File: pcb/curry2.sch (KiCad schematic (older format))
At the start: 6 parts

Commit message: Schematic almost done
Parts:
- added C? (x4): 10µF, symbol C
- added C? (x5): 0.1µF, symbol C
- added C? (x8): 4.7µF, symbol C
- added C?: 0.47µF, symbol C
- added C? (x2): 22pF, symbol C
- added IC?: ATMEGA88-A, TQFP32, symbol ATMEGA88-A
- added L? (x2): INDUCTOR, symbol INDUCTOR
- added X?: CRYSTAL, symbol CRYSTAL
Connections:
- net at U?.1 (3v3): now also L?.2
- net DB4: now reaches U?.10 (GPIO15)
- net DB5: now reaches U?.11 (GPIO17)
- net DB6: now reaches U?.12 (GPIO18)
- net DB7: now reaches U?.13 (GPIO27)
- net DB8: now reaches U?.15 (GPIO22)
- net DB9: now reaches U?.16 (GPIO23)
- net DB10: now reaches U?.18 (GPIO24)
- net DB11: now reaches U?.19 (GPIO10)
- net at U?.2 (5V): now also U?.4 (5V), L?.1
- net DB12: now reaches U?.21 (GPIO9)
- net DB13: now reaches U?.22 (GPIO25)
- net DB14: now reaches U?.23 (GPIO11)
- net DB15: now reaches U?.24 (GPIO8)
- net RD: now reaches U?.26 (GPIO7)
- net RD: now also U?.12 (RD)
- net SDA: now reaches U?.29 (GPIO28/I2C0_SDA)
- net SDA: now also IC?.27 ((PCINT12/SDA/ADC4)PC4)
- net BUSY/INT: now reaches U?.3 (GIPO2)
- net BUSY/INT: now also U?.35 (BUSY/INT), IC?.2 ((PCINT20/XCK/T0)PD4)
- net SCL: now reaches U?.30 (GPIO29/I2C0SCL)
- net SCL: now also IC?.28 ((PCINT14/SCL/ADC5)PC5)
- net CS: now reaches U?.31 (GPIO30)
- net CS: now also U?.13 (CS/FS)
- net DB0: now reaches U?.5 (GPIO3)
- net DB0: now also U?.33 (DB0)
- net GND: now reaches U?.6 (GND)
- net GND: now also U?.24 (DGND), C?.1, C?.1, C?.2, C?.2, C?.2, C?.2
- net DB1: now reaches U?.7 (GPIO4)
- net DB2: now reaches U?.8 (GPIO14)
- net DB3: now reaches U?.9 (GND)
- net HVSS: now reaches U?.1 (HVSS)
- net HVSS: now also C?.2, C?.2
- net RES: now reaches U?.10 (RESET)
- net RES: now also IC?.24 ((PCINT9/ADC1)PC1)
- net WR: now reaches U?.11 (REFN/WR)
- net WR: now also IC?.23 ((PCINT8/ADC0)PC0)
- net AVDD: now reaches U?.14 (AVDD)
- net AVDD: now also U?.4 (AVDD), U?.45 (AVDD), U?.52 (AVDD), U?.57 (AVDD), U?.61 (AVDD), C?.1, C?.1, C?.1, C?.1, C?.1, C?.1, C?.1, L?.2
- net AGND: now reaches U?.15 (AGND)
- net AGND: now also U?.44 (AGND), U?.5 (AGND), U?.51 (AGND), U?.55 (REFN), U?.58 (AGND), U?.62 (AGND), C?.1, C?.1, C?.2, C?.2, C?.2, C?.2
- net chAop/OUT2: now reaches U?.2 (CH_D1)
- net DVDD: now reaches U?.25 (DVDD)
- net DVDD: now also C?.1, C?.1, L?.1
- net RANGE: now reaches U?.34 (RANGE/XCLK)
- net RANGE: now also IC?.1 ((PCINT19/OC2B/INT1)PD3)
- net SLEEP: now reaches U?.36 (ASLEEP)
- net SLEEP: now also IC?.9 ((PCINT21/OC0B/T1)PD5)
- net CONVA: now reaches U?.37 (CONVST_A)
- net CONVA: now also IC?.12 ((PCINT0/CLKO/ICP1)PB0)
- net CONVB: now reaches U?.38 (CONVST_B)
- net CONVB: now also IC?.13 ((PCINT1/OC1A)PB1)
- net CONVC: now reaches U?.39 (CONVST_C)
- net CONVC: now also IC?.14 ((PCINT2/OC1B/~SS~)PB2)
- net CONVD: now reaches U?.40 (CONVST_D)
- net CONVD: now also IC?.15 ((PCINT3/OC2/MOSI)PB3)
- net HW: now reaches U?.41 (HW/SW)
- net HW: now also IC?.16 ((PCINT4/MISO)PB4)
- net chAop/OUT1: now reaches U?.42 (CH_A0)
- net chAop/OUT2: now reaches U?.47 (CH_A1)
- net HVDD: now reaches U?.48 (HVDD)
- net HVDD: now also C?.1, C?.1
- net chAop/OUT1: now reaches U?.49 (CH_B0)
- net chAop/OUT2: now reaches U?.54 (CH_B1)
- net at U?.56 (REFIO): now also C?.2
- net chAop/OUT2: now reaches U?.59 (CH_C1)
- net chAop/OUT1: now reaches U?.64 (CH_C0)
- net chAop/OUT1: now reaches U?.7 (CH_D0)
- net PAR: now reaches U?.8 (PAR_/SER)
- net PAR: now also IC?.26 ((PCINT11/ADC3)PC3)
- net STD: now reaches U?.9 (STDBY)
- net STD: now also IC?.25 ((PCINT10/ADC2)PC2)
- new net: C?.1, C?.2 (x3)
- new net: C?.2, IC?.7 ((PCINT6/XTAL1/TOSC1)PB6), X?.1
- new net: C?.2, IC?.8 ((PCINT7/XTAL2/TOSC2)PB7), X?.2
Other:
- moved on the sheet: C?, U?

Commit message: almost done rtc placed
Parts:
- added BT?: BATTERY, symbol BATTERY
- added C?: 1µF, symbol C
- added CON?: AVR-ISP-6, AVR-ISP-6, symbol AVR-ISP-6
- added L? (x3): INDUCTOR, symbol INDUCTOR
- added P?: CONN_2, symbol CONN_2
- added P?: CONN_4X2, symbol CONN_4X2
- added R? (x3): R, symbol R
- added U?: BQ32000, symbol BQ32000
- added X?: CRYSTAL, symbol CRYSTAL
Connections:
- net chAop/OUT1 is gone; now on net chAop/OUT1: U?.7 (CH_D0)
- net chAop/OUT2 is gone; now on net chAop/OUT2: U?.59 (CH_C1)
- net AVDD: now also L?.1, L?.1; no longer L?.2
- net CONVA: now also P?.7
- net CONVB: now also P?.5
- net CONVC: now also P?.3
- net CONVD: now also CON?.4, P?.1
- net DVDD: now also IC?.4 (VCC), IC?.6 (VCC), C?.1, R?.1, R?.1, R?.1, U?.8 (VCC)
- net GND: now also IC?.3 (GND), U?.20 (GND), U?.25 (GND), U?.33 (GND), U?.34 (GND), U?.35 (GND), BT?.2 (-), C?.2, U?.4 (GND)
- net HW: now also CON?.1
- net SCL: now also U?.6 (SCL)
- net SDA: now also U?.5 (SDA)
- net chAop/OUT1: no longer U?.42 (CH_A0)
- net chAop/OUT2: no longer U?.2 (CH_D1)
- net power/+5: now also P?.1 (P1)
- net power/Enable: now also IC?.30 ((PCINT16/RXD)PD0)
- net power/GND: now also P?.2 (PM)
- net at L?.2, U?.1 (3v3): now also U?.17 (3V3)
- net at L?.1, U?.2 (5V), U?.4 (5V): now also L?.1
- net at IC?.11 ((PCINT23/AIN1)PD7): now also P?.2, P?.8
- net at IC?.17 ((PCINT5/SCK)PB5): now also CON?.3
- net RST: now reaches IC?.29 ((PCINT14/~RESET~)PC6)
- net RST: now also CON?.5, R?.2
- new net: L?.2, L?.2
- new net: U?.2 (OSCI), X?.2
- new net: BT?.1 (+), U?.3 (VBAT)
- new net: U?.3 (VBAT), X?.1
- new net chAop/OUT1: U?.42 (CH_A0)
- new net chAop/OUT2: U?.2 (CH_D1)
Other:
- moved on the sheet: C?, IC?, L?, X?

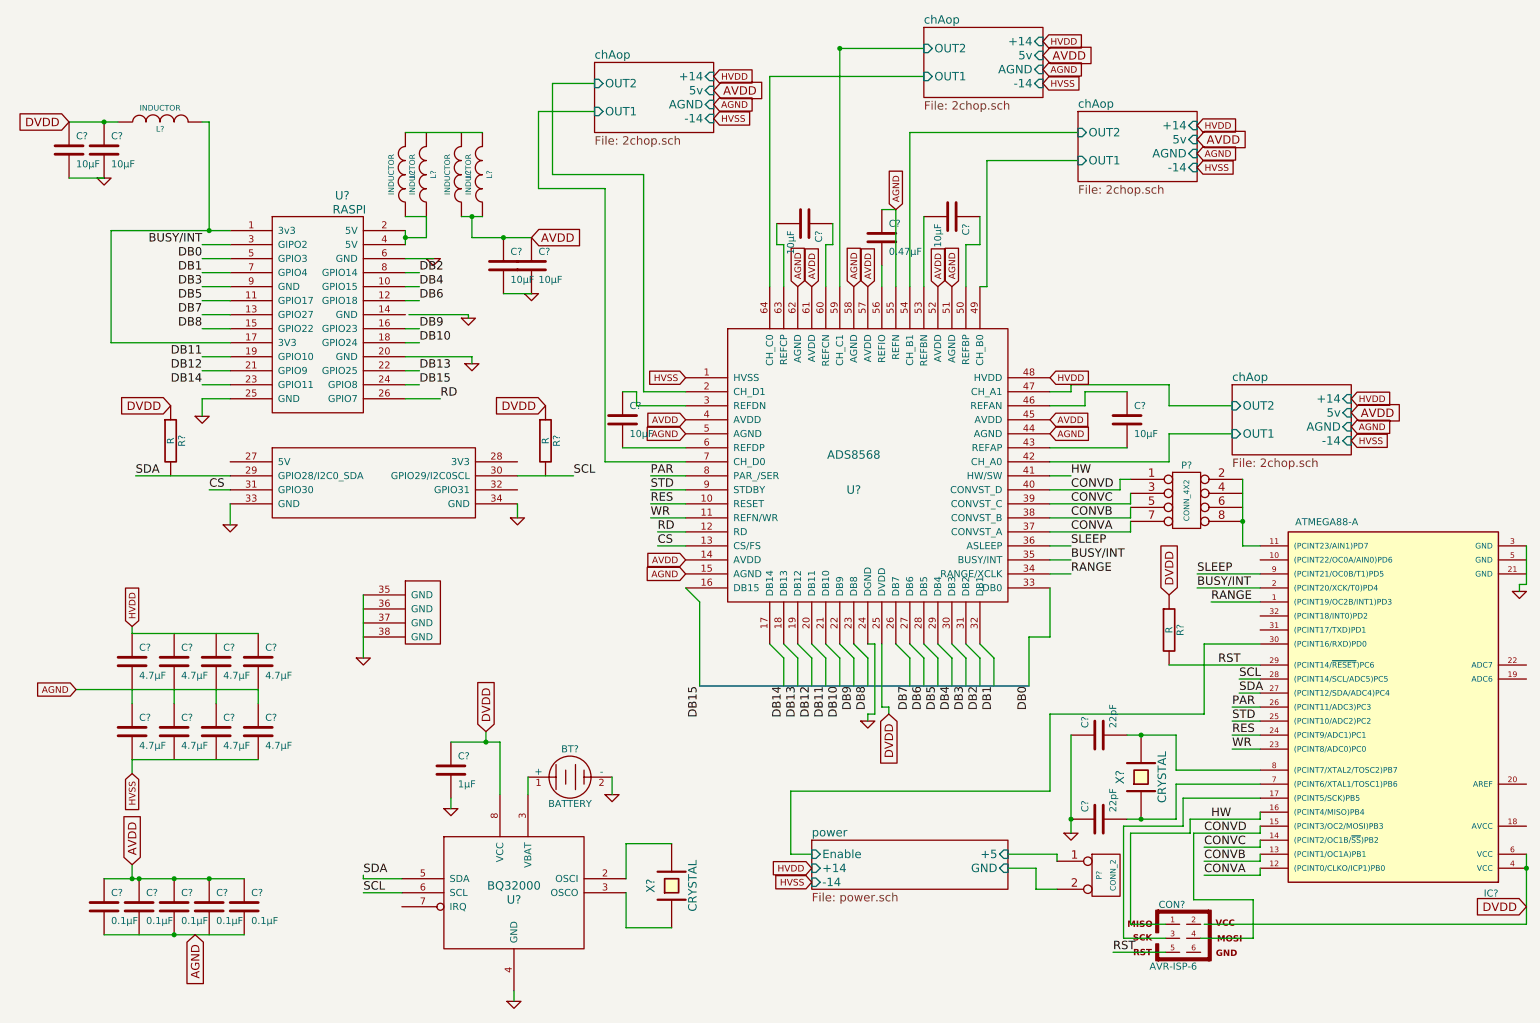
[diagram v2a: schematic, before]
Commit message: fixed all pcb components
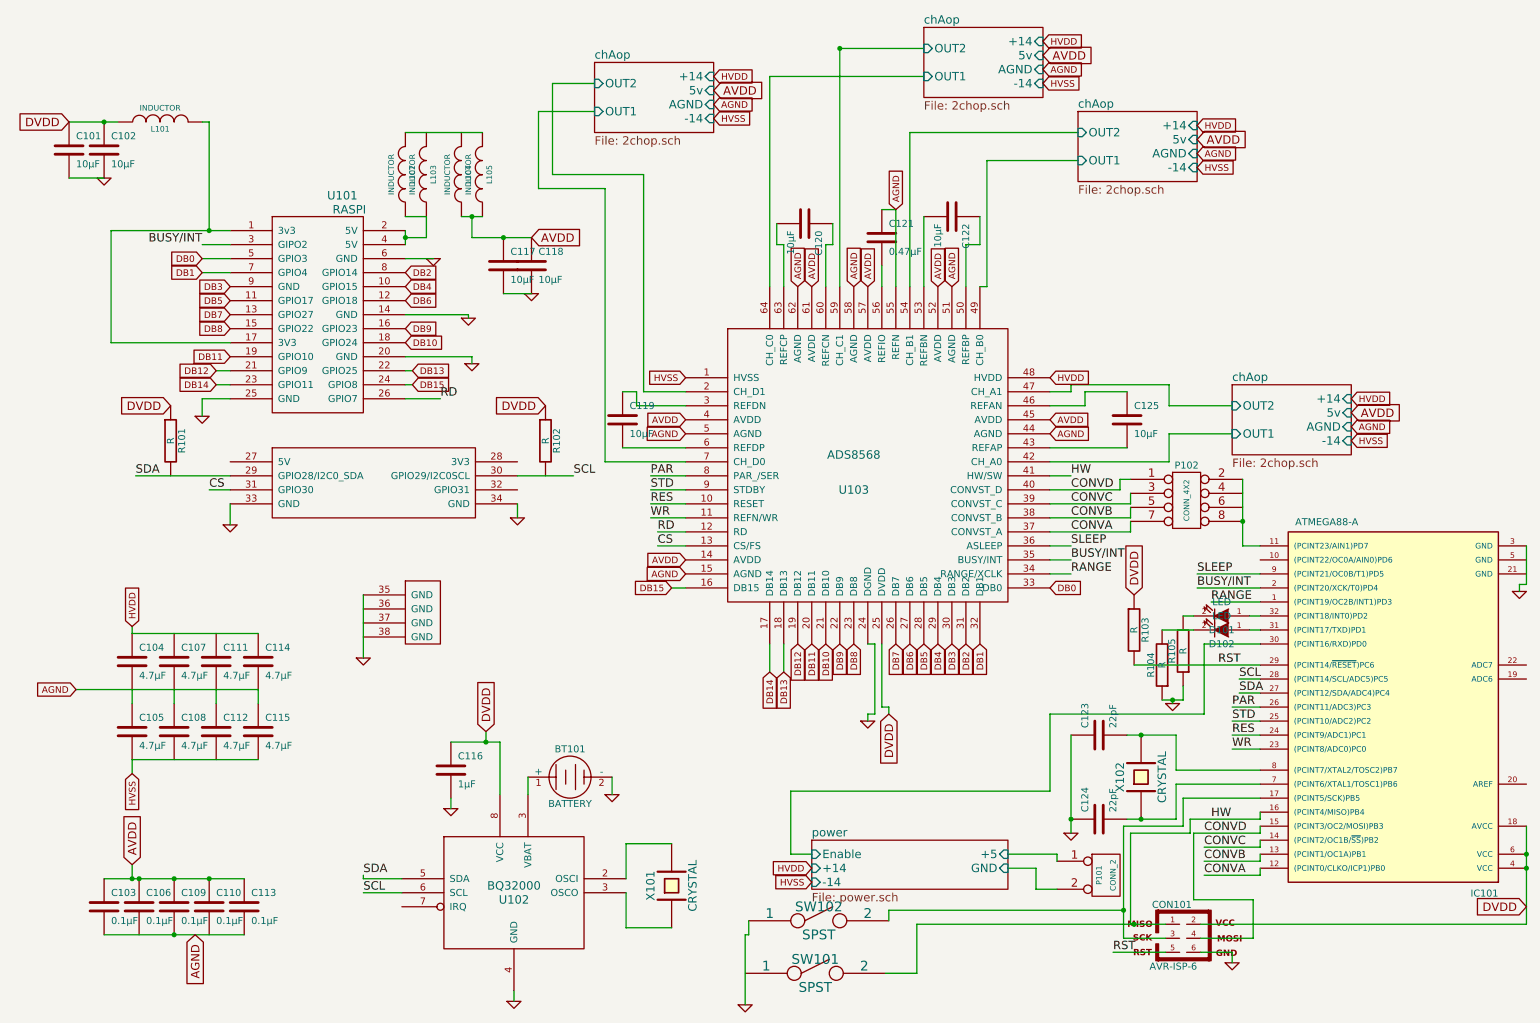
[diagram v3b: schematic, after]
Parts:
- added D101, D102: LED, symbol LED
- added R104, R105: R, symbol R
- added SW101, SW102: SPST, symbol SPST
- gave numbers to parts that had none: 43
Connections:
- net chAop/OUT1 is gone; now on net chAop/OUT1: U103.7 (CH_D0)
- net chAop/OUT2 is gone; now on net chAop/OUT2: U103.59 (CH_C1)
- net DB1: now also U103.32 (DB1)
- net DB10: now also U103.21 (DB10)
- net DB11: now also U103.20 (DB11)
- net DB12: now also U103.19 (DB12)
- net DB13: now also U103.18 (DB13)
- net DB14: now also U103.17 (DB14)
- net DB15: now also U103.16 (DB15)
- net DB2: now also U103.31 (DB2)
- net DB3: now also U103.30 (DB3)
- net DB4: now also U103.29 (DB4)
- net DB5: now also U103.28 (DB5)
- net DB6: now also U103.27 (DB6)
- net DB7: now also U103.26 (DB7)
- net DB8: now also U103.23 (DB8)
- net DB9: now also U103.22 (DB9)
- net DVDD: now also CON101.2, IC101.18 (AVCC)
- net GND: now also CON101.6, U101.14 (GND), R104.1, R105.1, SW102.1
- net HW: now also SW101.2
- net chAop/OUT1: no longer U103.42 (CH_A0)
- net chAop/OUT2: no longer U103.2 (CH_D1)
- net at CON101.3, IC101.17 ((PCINT5/SCK)PB5): now also SW102.2
- net at IC101.31 ((PCINT17/TXD)PD1): now also D102.1 (A)
- net at IC101.32 ((PCINT18/INT0)PD2): now also D101.1 (A)
- new net: D101.2 (K), R105.2
- new net: D102.2 (K), R104.2
- new net chAop/OUT1: U103.42 (CH_A0)
- new net chAop/OUT2: U103.2 (CH_D1)
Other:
- moved on the sheet: R103
